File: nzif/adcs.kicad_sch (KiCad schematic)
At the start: 26 parts, among them U401 ADA4807-1, U402 ADAU1979xBCP

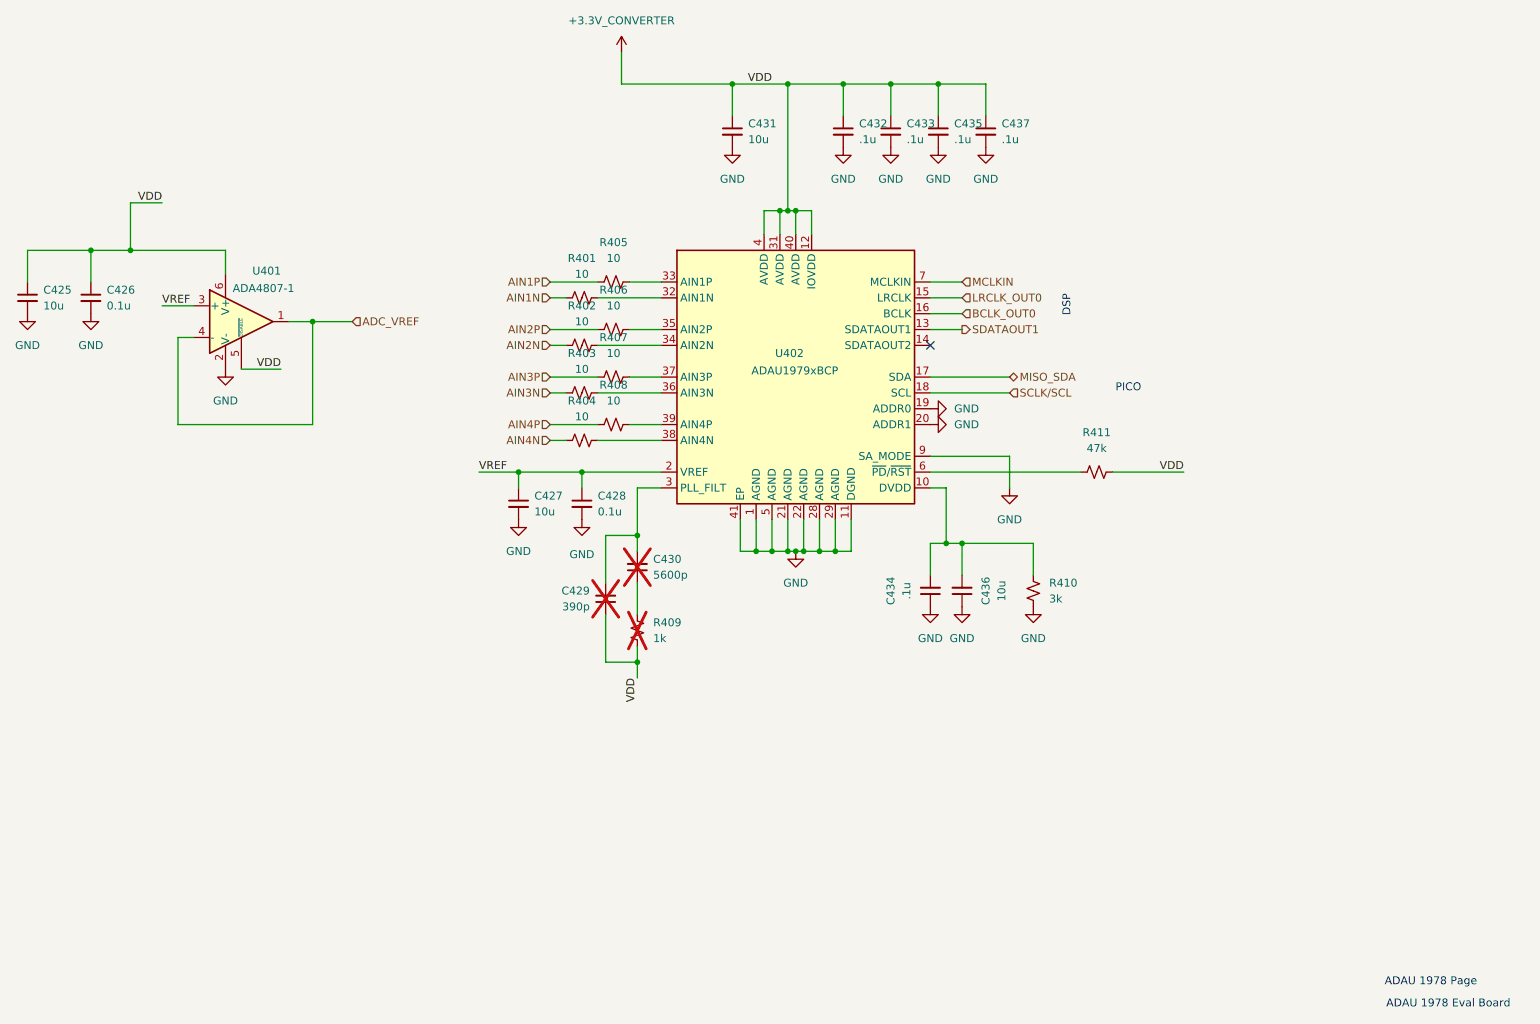
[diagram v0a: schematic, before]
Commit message: top sheet wiring
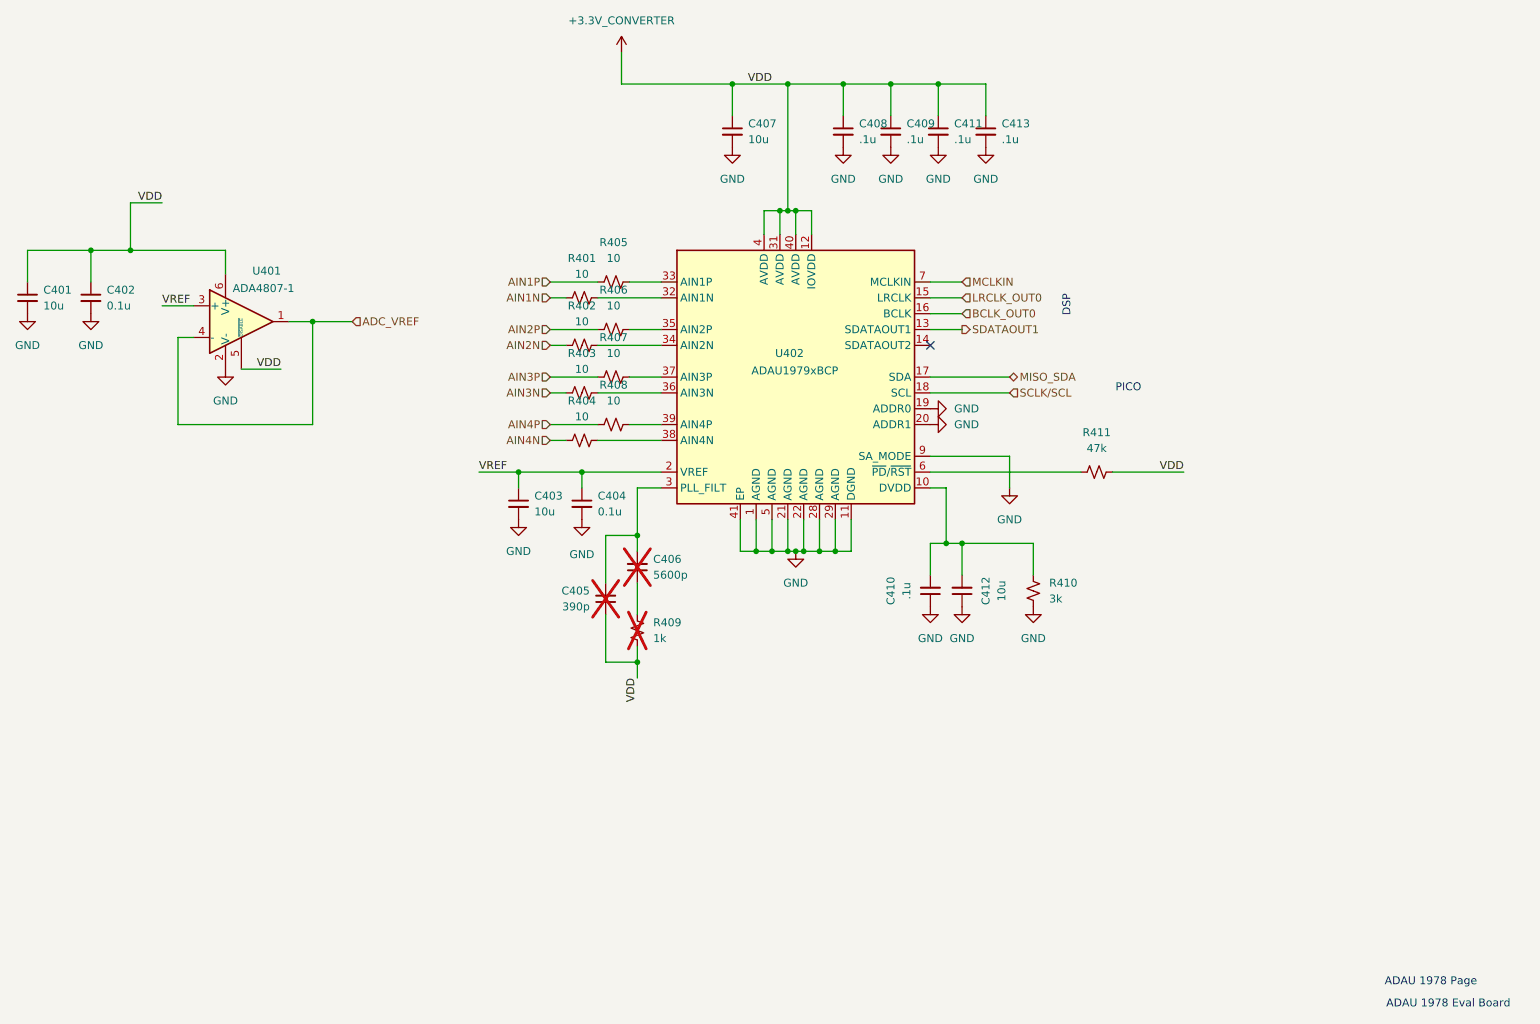
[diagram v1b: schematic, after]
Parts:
- renumbered C425 to C401, C426 to C402, C427 to C403, C428 to C404, C429 to C405, C430 to C406, C431 to C407, C432 to C408, C433 to C409, C434 to C410, C435 to C411, C436 to C412, C437 to C413
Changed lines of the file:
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@@
 		(dnp no)
 		(fields_autoplaced yes)
-		(property "Reference" "C426"
+		(property "Reference" "C402"
 			(at 107.95 116.8462 0)
 			(show_name no)
@@
 			(project "nzif"
 				(path "/fe42ca2f-2bb8-4d5a-9e84-807788ed632f/d1b276aa-cc76-4829-b01b-98095216e3ce"
-					(reference "C426")
+					(reference "C402")
 					(unit 1)
 				)
@@
 		(dnp no)
 		(fields_autoplaced yes)
-		(property "Reference" "C435"
+		(property "Reference" "C411"
 			(at 243.84 90.1762 0)
 			(show_name no)
@@
 			(project "nzif"
 				(path "/fe42ca2f-2bb8-4d5a-9e84-807788ed632f/d1b276aa-cc76-4829-b01b-98095216e3ce"
-					(reference "C435")
+					(reference "C411")
 					(unit 1)
 				)
@@
 		(dnp yes)
 		(fields_autoplaced yes)
-		(property "Reference" "C430"
+		(property "Reference" "C406"
 			(at 195.58 160.0135 0)
 			(show_name no)
@@
 			(project "nzif"
 				(path "/fe42ca2f-2bb8-4d5a-9e84-807788ed632f/d1b276aa-cc76-4829-b01b-98095216e3ce"
-					(reference "C430")
+					(reference "C406")
 					(unit 1)
 				)
@@
 		(dnp no)
 		(fields_autoplaced yes)
-		(property "Reference" "C434"
+		(property "Reference" "C410"
 			(at 233.68 165.0937 90)
 			(show_name no)
@@
 			(project "nzif"
 				(path "/fe42ca2f-2bb8-4d5a-9e84-807788ed632f/d1b276aa-cc76-4829-b01b-98095216e3ce"
-					(reference "C434")
+					(reference "C410")
 					(unit 1)
 				)
@@
 		(dnp no)
 		(fields_autoplaced yes)
-		(property "Reference" "C427"
+		(property "Reference" "C403"
 			(at 176.53 149.8662 0)
 			(show_name no)
@@
 			(project "nzif"
 				(path "/fe42ca2f-2bb8-4d5a-9e84-807788ed632f/d1b276aa-cc76-4829-b01b-98095216e3ce"
-					(reference "C427")
+					(reference "C403")
 					(unit 1)
 				)
@@
 		(in_pos_files yes)
 		(dnp yes)
-		(property "Reference" "C429"
+		(property "Reference" "C405"
 			(at 185.42 165.0935 0)
 			(show_name no)
@@
 			(project "nzif"
 				(path "/fe42ca2f-2bb8-4d5a-9e84-807788ed632f/d1b276aa-cc76-4829-b01b-98095216e3ce"
-					(reference "C429")
+					(reference "C405")
 					(unit 1)
 				)
@@
 		(dnp no)
 		(fields_autoplaced yes)
-		(property "Reference" "C425"
+		(property "Reference" "C401"
 			(at 97.79 116.8462 0)
 			(show_name no)
@@
 			(project "nzif"
 				(path "/fe42ca2f-2bb8-4d5a-9e84-807788ed632f/d1b276aa-cc76-4829-b01b-98095216e3ce"
-					(reference "C425")
+					(reference "C401")
 					(unit 1)
 				)
@@
 		(dnp no)
 		(fields_autoplaced yes)
-		(property "Reference" "C437"
+		(property "Reference" "C413"
 			(at 251.46 90.1762 0)
 			(show_name no)
@@
 			(project "nzif"
 				(path "/fe42ca2f-2bb8-4d5a-9e84-807788ed632f/d1b276aa-cc76-4829-b01b-98095216e3ce"
-					(reference "C437")
+					(reference "C413")
 					(unit 1)
 				)
@@
 		(dnp no)
 		(fields_autoplaced yes)
-		(property "Reference" "C431"
+		(property "Reference" "C407"
 			(at 210.82 90.1762 0)
 			(show_name no)
@@
 			(project "nzif"
 				(path "/fe42ca2f-2bb8-4d5a-9e84-807788ed632f/d1b276aa-cc76-4829-b01b-98095216e3ce"
-					(reference "C431")
+					(reference "C407")
 					(unit 1)
 				)
@@
 		(dnp no)
 		(fields_autoplaced yes)
-		(property "Reference" "C436"
+		(property "Reference" "C412"
 			(at 248.92 165.0937 90)
 			(show_name no)
@@
 			(project "nzif"
 				(path "/fe42ca2f-2bb8-4d5a-9e84-807788ed632f/d1b276aa-cc76-4829-b01b-98095216e3ce"
-					(reference "C436")
+					(reference "C412")
 					(unit 1)
 				)
@@
 		(dnp no)
 		(fields_autoplaced yes)
-		(property "Reference" "C432"
+		(property "Reference" "C408"
 			(at 228.6 90.1762 0)
 			(show_name no)
@@
 			(project "nzif"
 				(path "/fe42ca2f-2bb8-4d5a-9e84-807788ed632f/d1b276aa-cc76-4829-b01b-98095216e3ce"
-					(reference "C432")
+					(reference "C408")
 					(unit 1)
 				)
@@
 		(dnp no)
 		(fields_autoplaced yes)
-		(property "Reference" "C433"
+		(property "Reference" "C409"
 			(at 236.22 90.1762 0)
 			(show_name no)
@@
 			(project "nzif"
 				(path "/fe42ca2f-2bb8-4d5a-9e84-807788ed632f/d1b276aa-cc76-4829-b01b-98095216e3ce"
-					(reference "C433")
+					(reference "C409")
 					(unit 1)
 				)
@@
 		(dnp no)
 		(fields_autoplaced yes)
-		(property "Reference" "C428"
+		(property "Reference" "C404"
 			(at 186.69 149.8662 0)
 			(show_name no)
@@
 			(project "nzif"
 				(path "/fe42ca2f-2bb8-4d5a-9e84-807788ed632f/d1b276aa-cc76-4829-b01b-98095216e3ce"
-					(reference "C428")
+					(reference "C404")
 					(unit 1)
 				)

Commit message: updates to top level
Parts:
- added R1214: 49.9, symbol Device:R_Small_US
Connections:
- net MCLKIN: now also R1214.2; no longer U402.7 (MCLKIN)
- new net: R1214.1, U402.7 (MCLKIN)
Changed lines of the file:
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@@
 	(hierarchical_label "MCLKIN"
 		(shape input)
-		(at 245.11 115.57 0)
+		(at 250.19 115.57 0)
 		(effects
 			(font
@@
 					(unit 1)
 				)
+			)
+		)
+	)
+	(symbol
+		(lib_id "Device:R_Small_US")
+		(at 247.65 115.57 90)
+		(unit 1)
+		(body_style 1)
+		(exclude_from_sim no)
+		(in_bom yes)
+		(on_board yes)
+		(in_pos_files yes)
+		(dnp no)
+		(fields_autoplaced yes)
+		(property "Reference" "R1214"
+			(at 247.65 109.22 90)
+			(show_name no)
+			(do_not_autoplace no)
+			(effects
+				(font
+					(size 1.27 1.27)
+				)
+			)
+		)
+		(property "Value" "49.9"
+			(at 247.65 111.76 90)
+			(show_name no)
+			(do_not_autoplace no)
+			(effects
+				(font
+					(size 1.27 1.27)
+				)
+			)
+		)
+		(property "Footprint" ""
+			(at 247.65 115.57 0)
+			(hide yes)
+			(show_name no)
+			(do_not_autoplace no)
+			(effects
+				(font
+					(size 1.27 1.27)
+				)
+			)
+		)
+		(property "Datasheet" ""
+			(at 247.65 115.57 0)
+			(hide yes)
+			(show_name no)
+			(do_not_autoplace no)
+			(effects
+				(font
+					(size 1.27 1.27)
+				)
+			)
+		)
+		(property "Description" "Resistor, small US symbol"
+			(at 247.65 115.57 0)
+			(hide yes)
+			(show_name no)
+			(do_not_autoplace no)
+			(effects
+				(font
+					(size 1.27 1.27)
+				)
+			)
+		)
+		(pin "2"
+		)
+		(pin "1"
+		)
+		(instances
+			(project "nzif"
+				(path "/fe42ca2f-2bb8-4d5a-9e84-807788ed632f/d1b276aa-cc76-4829-b01b-98095216e3ce"
+					(reference "R1214")
+					(unit 1)
+				)

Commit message: Fix ERC errors: symbol pin types and schematic corrections
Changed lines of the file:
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@@
 	)
 	(junction
+		(at 134.62 129.54)
+		(diameter 0)
+		(color 0 0 0 0)
+	)
+	(junction
 		(at 173.99 146.05)
 		(diameter 0)
@@
 	(wire
 		(pts
+			(xy 134.62 129.54) (xy 135.89 129.54)
+		)
+		(stroke
+			(width 0)
+			(type default)
+		)
+	)
+	(wire
+		(pts
 			(xy 140.97 121.92) (xy 140.97 138.43)
 		)
@@
 	(wire
 		(pts
-			(xy 129.54 129.54) (xy 135.89 129.54)
+			(xy 129.54 129.54) (xy 134.62 129.54)
 		)
 		(stroke
@@
 	)
 	(label "VDD"
-		(at 135.89 129.54 180)
-		(effects
-			(font
-				(size 1.27 1.27)
-			)
-			(justify right bottom)
-		)
-	)
-	(label "VDD"
 		(at 193.04 179.07 270)
 		(effects
@@
 	)
 	(label "VDD"
+		(at 135.89 129.54 0)
+		(effects
+			(font
+				(size 1.27 1.27)
+			)
+			(justify left bottom)
+		)
+	)
+	(label "VDD"
 		(at 280.67 146.05 180)
 		(effects
@@
 					(unit 1)
 				)
+			)
+		)
+	)
+	(symbol
+		(lib_id "power:PWR_FLAG")
+		(at 134.62 129.54 180)
+		(unit 1)
+		(body_style 1)
+		(exclude_from_sim no)
+		(in_bom yes)
+		(on_board yes)
+		(in_pos_files yes)
+		(dnp no)
+		(fields_autoplaced yes)
+		(property "Reference" "#FLG01205"
+			(at 134.62 131.445 0)
+			(hide yes)
+			(show_name no)
+			(do_not_autoplace no)
+			(effects
+				(font
+					(size 1.27 1.27)
+				)
+			)
+		)
+		(property "Value" "PWR_FLAG"
+			(at 134.62 134.62 0)
+			(show_name no)
+			(do_not_autoplace no)
+			(effects
+				(font
+					(size 1.27 1.27)
+				)
+			)
+		)
+		(property "Footprint" ""
+			(at 134.62 129.54 0)
+			(hide yes)
+			(show_name no)
+			(do_not_autoplace no)
+			(effects
+				(font
+					(size 1.27 1.27)
+				)
+			)
+		)
+		(property "Datasheet" ""
+			(at 134.62 129.54 0)
+			(hide yes)
+			(show_name no)
+			(do_not_autoplace no)
+			(effects
+				(font
+					(size 1.27 1.27)
+				)
+			)
+		)
+		(property "Description" "Special symbol for telling ERC where power comes from"
+			(at 134.62 129.54 0)
+			(hide yes)
+			(show_name no)
+			(do_not_autoplace no)
+			(effects
+				(font
+					(size 1.27 1.27)
+				)
+			)
+		)
+		(pin "1"
+		)
+		(instances
+			(project "nzif"
+				(path "/fe42ca2f-2bb8-4d5a-9e84-807788ed632f/d1b276aa-cc76-4829-b01b-98095216e3ce"
+					(reference "#FLG01205")
+					(unit 1)
+				)

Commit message: erc improvements
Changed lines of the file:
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@@
-	(wire
-		(pts
-			(xy 213.36 107.95) (xy 213.36 104.14)
-		)
-		(stroke
-			(width 0)
-			(type default)
-		)
-	)
 	(wire
 		(pts
@@
 		(pts
 			(xy 209.55 158.75) (xy 212.09 158.75)
+		)
+		(stroke
+			(width 0)
+			(type default)
+		)
+	)
+	(wire
+		(pts
+			(xy 213.36 104.14) (xy 213.36 107.95)
 		)
 		(stroke
@@
 	)
 	(label "VDD"
-		(at 214.63 83.82 180)
+		(at 196.85 83.82 180)
 		(effects
 			(font

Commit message: fixed error with selfboot circuit
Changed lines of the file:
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@@
 	)
 	(junction
+		(at 193.04 176.53)
+		(diameter 0)
+		(color 0 0 0 0)
+	)
+	(junction
 		(at 193.04 156.21)
 		(diameter 0)
@@
 	)
 	(junction
-		(at 217.17 83.82)
+		(at 127 110.49)
 		(diameter 0)
 		(color 0 0 0 0)
 	)
 	(junction
-		(at 218.44 104.14)
+		(at 217.17 83.82)
 		(diameter 0)
 		(color 0 0 0 0)
 	)
 	(junction
-		(at 134.62 129.54)
+		(at 218.44 104.14)
 		(diameter 0)
 		(color 0 0 0 0)
@@
 	)
 	(junction
-		(at 193.04 176.53)
+		(at 248.92 83.82)
 		(diameter 0)
 		(color 0 0 0 0)
@@
 	(wire
 		(pts
-			(xy 134.62 129.54) (xy 135.89 129.54)
-		)
-		(stroke
-			(width 0)
-			(type default)
-		)
-	)
-	(wire
-		(pts
 			(xy 140.97 121.92) (xy 140.97 138.43)
 		)
@@
 	(wire
 		(pts
+			(xy 193.04 176.53) (xy 205.74 176.53)
+		)
+		(stroke
+			(width 0)
+			(type default)
+		)
+	)
+	(wire
+		(pts
 			(xy 214.63 153.67) (xy 214.63 158.75)
 		)
@@
 	(wire
 		(pts
-			(xy 111.76 110.49) (xy 111.76 102.87)
+			(xy 111.76 101.6) (xy 111.76 110.49)
 		)
 		(stroke
@@
 	(wire
 		(pts
+			(xy 280.67 146.05) (xy 280.67 83.82)
+		)
+		(stroke
+			(width 0)
+			(type default)
+		)
+	)
+	(wire
+		(pts
 			(xy 240.03 157.48) (xy 242.57 157.48)
 		)
@@
 	(wire
 		(pts
-			(xy 129.54 129.54) (xy 134.62 129.54)
+			(xy 269.24 146.05) (xy 280.67 146.05)
 		)
 		(stroke
@@
 	(wire
 		(pts
-			(xy 269.24 146.05) (xy 280.67 146.05)
+			(xy 212.09 153.67) (xy 212.09 158.75)
 		)
 		(stroke
@@
 	(wire
 		(pts
-			(xy 212.09 153.67) (xy 212.09 158.75)
+			(xy 208.28 83.82) (xy 217.17 83.82)
 		)
 		(stroke
@@
 	(wire
 		(pts
-			(xy 208.28 83.82) (xy 217.17 83.82)
+			(xy 129.54 129.54) (xy 138.43 129.54)
 		)
 		(stroke
@@
 	(wire
 		(pts
+			(xy 127 110.49) (xy 138.43 110.49)
+		)
+		(stroke
+			(width 0)
+			(type default)
+		)
+	)
+	(wire
+		(pts
 			(xy 179.07 140.97) (xy 181.61 140.97)
 		)
@@
 	(wire
 		(pts
+			(xy 280.67 83.82) (xy 248.92 83.82)
+		)
+		(stroke
+			(width 0)
+			(type default)
+		)
+	)
+	(wire
+		(pts
 			(xy 213.36 104.14) (xy 213.36 107.95)
 		)
@@
 	(wire
 		(pts
+			(xy 205.74 170.18) (xy 205.74 176.53)
+		)
+		(stroke
+			(width 0)
+			(type default)
+		)
+	)
+	(wire
+		(pts
 			(xy 191.77 123.19) (xy 196.85 123.19)
 		)
@@
 	(wire
 		(pts
-			(xy 193.04 176.53) (xy 193.04 179.07)
-		)
-		(stroke
-			(width 0)
-			(type default)
-		)
-	)
-	(wire
-		(pts
 			(xy 215.9 104.14) (xy 215.9 107.95)
 		)
@@
 	(wire
 		(pts
-			(xy 111.76 102.87) (xy 116.84 102.87)
+			(xy 256.54 162.56) (xy 256.54 157.48)
 		)
 		(stroke
@@
 	(wire
 		(pts
-			(xy 256.54 162.56) (xy 256.54 157.48)
+			(xy 138.43 129.54) (xy 138.43 110.49)
 		)
 		(stroke
@@
 		)
 	)
-	(label "VDD"
-		(at 193.04 179.07 270)
-		(effects
-			(font
-				(size 1.27 1.27)
-			)
-			(justify right bottom)
-		)
-	)
-	(label "VDD"
-		(at 116.84 102.87 180)
-		(effects
-			(font
-				(size 1.27 1.27)
-			)
-			(justify right bottom)
-		)
-	)
 	(label "VREF"
 		(at 167.64 146.05 0)
@@
 		)
 	)
-	(label "VDD"
-		(at 196.85 83.82 180)
-		(effects
-			(font
-				(size 1.27 1.27)
-			)
-			(justify right bottom)
-		)
-	)
-	(label "VDD"
-		(at 135.89 129.54 0)
-		(effects
-			(font
-				(size 1.27 1.27)
-			)
-			(justify left bottom)
-		)
-	)
-	(label "VDD"
-		(at 280.67 146.05 180)
-		(effects
-			(font
-				(size 1.27 1.27)
-			)
-			(justify right bottom)
-		)
-	)
 	(hierarchical_label "AIN1N"
 		(shape input)
@@
 	)
 	(symbol
+		(lib_id "power:+3.3V")
+		(at 205.74 170.18 0)
+		(unit 1)
+		(body_style 1)
+		(exclude_from_sim no)
+		(in_bom yes)
+		(on_board yes)
+		(in_pos_files yes)
+		(dnp no)
+		(fields_autoplaced yes)
+		(property "Reference" "#PWR0420"
+			(at 205.74 173.99 0)
+			(hide yes)
+			(show_name no)
+			(do_not_autoplace no)
+			(effects
+				(font
+					(size 1.27 1.27)
+				)
+			)
+		)
+		(property "Value" "+3.3V_CONVERTER"
+			(at 205.74 165.1 0)
+			(show_name no)
+			(do_not_autoplace no)
+			(effects
+				(font
+					(size 1.27 1.27)
+				)
+			)
+		)
+		(property "Footprint" ""
+			(at 205.74 170.18 0)
+			(hide yes)
+			(show_name no)
+			(do_not_autoplace no)
+			(effects
+				(font
+					(size 1.27 1.27)
+				)
+			)
+		)
+		(property "Datasheet" ""
+			(at 205.74 170.18 0)
+			(hide yes)
+			(show_name no)
+			(do_not_autoplace no)
+			(effects
+				(font
+					(size 1.27 1.27)
+				)
+			)
+		)
+		(property "Description" "Power symbol creates a global label with name \"+3.3V\""
+			(at 205.74 170.18 0)
+			(hide yes)
+			(show_name no)
+			(do_not_autoplace no)
+			(effects
+				(font
+					(size 1.27 1.27)
+				)
+			)
+		)
+		(pin "1"
+		)
+		(instances
+			(project "nzif"
+				(path "/fe42ca2f-2bb8-4d5a-9e84-807788ed632f/d1b276aa-cc76-4829-b01b-98095216e3ce"
+					(reference "#PWR0420")
+					(unit 1)
+				)
+			)
+		)
+	)
+	(symbol
 		(lib_id "power:GND")
 		(at 240.03 135.89 90)
@@
 	)
 	(symbol
+		(lib_id "power:+3.3V")
+		(at 111.76 101.6 0)
+		(unit 1)
+		(body_style 1)
+		(exclude_from_sim no)
+		(in_bom yes)
+		(on_board yes)
+		(in_pos_files yes)
+		(dnp no)
+		(fields_autoplaced yes)
+		(property "Reference" "#PWR0419"
+			(at 111.76 105.41 0)
+			(hide yes)
+			(show_name no)
+			(do_not_autoplace no)
+			(effects
+				(font
+					(size 1.27 1.27)
+				)
+			)
+		)
+		(property "Value" "+3.3V_CONVERTER"
+			(at 111.76 96.52 0)
+			(show_name no)
+			(do_not_autoplace no)
+			(effects
+				(font
+					(size 1.27 1.27)
+				)
+			)
+		)
+		(property "Footprint" ""
+			(at 111.76 101.6 0)
+			(hide yes)
+			(show_name no)
+			(do_not_autoplace no)
+			(effects
+				(font
+					(size 1.27 1.27)
+				)
+			)
+		)
+		(property "Datasheet" ""
+			(at 111.76 101.6 0)
+			(hide yes)
+			(show_name no)
+			(do_not_autoplace no)
+			(effects
+				(font
+					(size 1.27 1.27)
+				)
+			)
+		)
+		(property "Description" "Power symbol creates a global label with name \"+3.3V\""
+			(at 111.76 101.6 0)
+			(hide yes)
+			(show_name no)
+			(do_not_autoplace no)
+			(effects
+				(font
+					(size 1.27 1.27)
+				)
+			)
+		)
+		(pin "1"
+		)
+		(instances
+			(project "nzif"
+				(path "/fe42ca2f-2bb8-4d5a-9e84-807788ed632f/d1b276aa-cc76-4829-b01b-98095216e3ce"
+					(reference "#PWR0419")
+					(unit 1)
+				)
+			)
+		)
+	)
+	(symbol
 		(lib_id "power:GND")
 		(at 240.03 167.64 0)
@@
 					(unit 1)
 				)
-			)
-		)
-	)
-	(symbol
-		(lib_id "power:PWR_FLAG")
-		(at 134.62 129.54 180)
-		(unit 1)
-		(body_style 1)
-		(exclude_from_sim no)
-		(in_bom yes)
-		(on_board yes)
-		(in_pos_files yes)
-		(dnp no)
-		(fields_autoplaced yes)
-		(property "Reference" "#FLG01205"
-			(at 134.62 131.445 0)
-			(hide yes)
-			(show_name no)
-			(do_not_autoplace no)
-			(effects
-				(font
-					(size 1.27 1.27)
-				)
-			)
-		)
-		(property "Value" "PWR_FLAG"
-			(at 134.62 134.62 0)
-			(show_name no)
-			(do_not_autoplace no)
-			(effects
-				(font
-					(size 1.27 1.27)
-				)
-			)
-		)
-		(property "Footprint" ""
-			(at 134.62 129.54 0)
-			(hide yes)
-			(show_name no)
-			(do_not_autoplace no)
-			(effects
-				(font
-					(size 1.27 1.27)
-				)
-			)
-		)
-		(property "Datasheet" ""
-			(at 134.62 129.54 0)
-			(hide yes)
-			(show_name no)
-			(do_not_autoplace no)
-			(effects
-				(font
-					(size 1.27 1.27)
-				)
-			)
-		)
-		(property "Description" "Special symbol for telling ERC where power comes from"
-			(at 134.62 129.54 0)
-			(hide yes)
-			(show_name no)
-			(do_not_autoplace no)
-			(effects
-				(font
-					(size 1.27 1.27)
-				)
-			)
-		)
-		(pin "1"
-		)
-		(instances
-			(project "nzif"
-				(path "/fe42ca2f-2bb8-4d5a-9e84-807788ed632f/d1b276aa-cc76-4829-b01b-98095216e3ce"
-					(reference "#FLG01205")
-					(unit 1)
-				)
